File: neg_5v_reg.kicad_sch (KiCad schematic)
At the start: 33 parts, among them U2 SIC461ED-T1-GE3

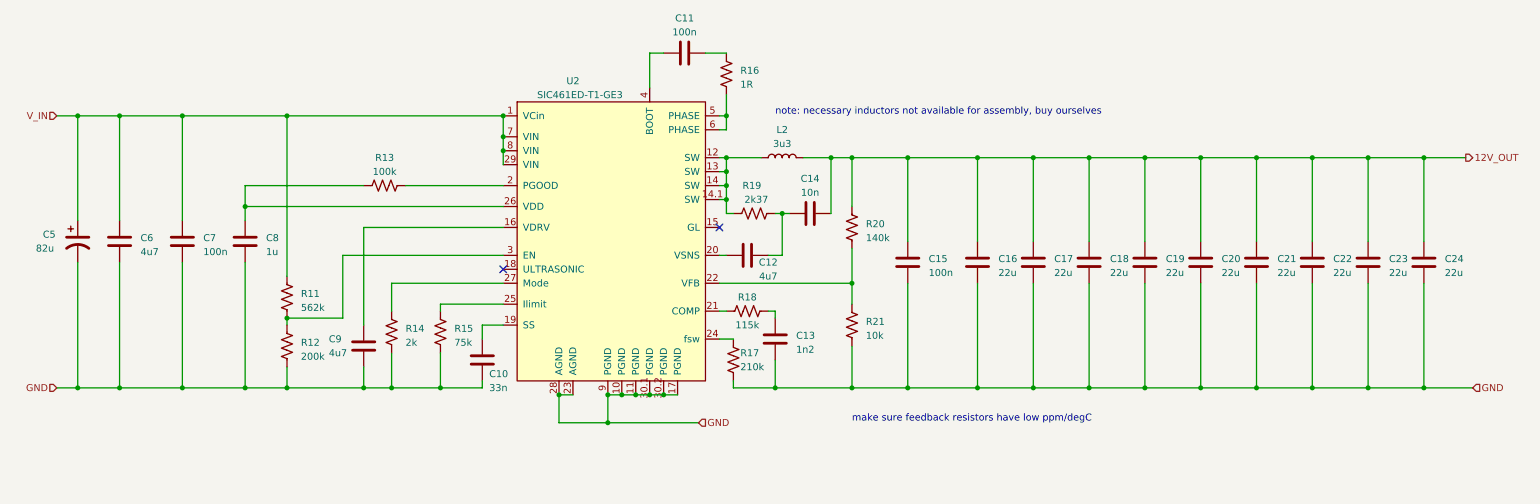
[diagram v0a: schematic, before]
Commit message: Added -5V voltage source using 5V regulator, also fixed 3V3 output pins on 3V3 regulator subsheets
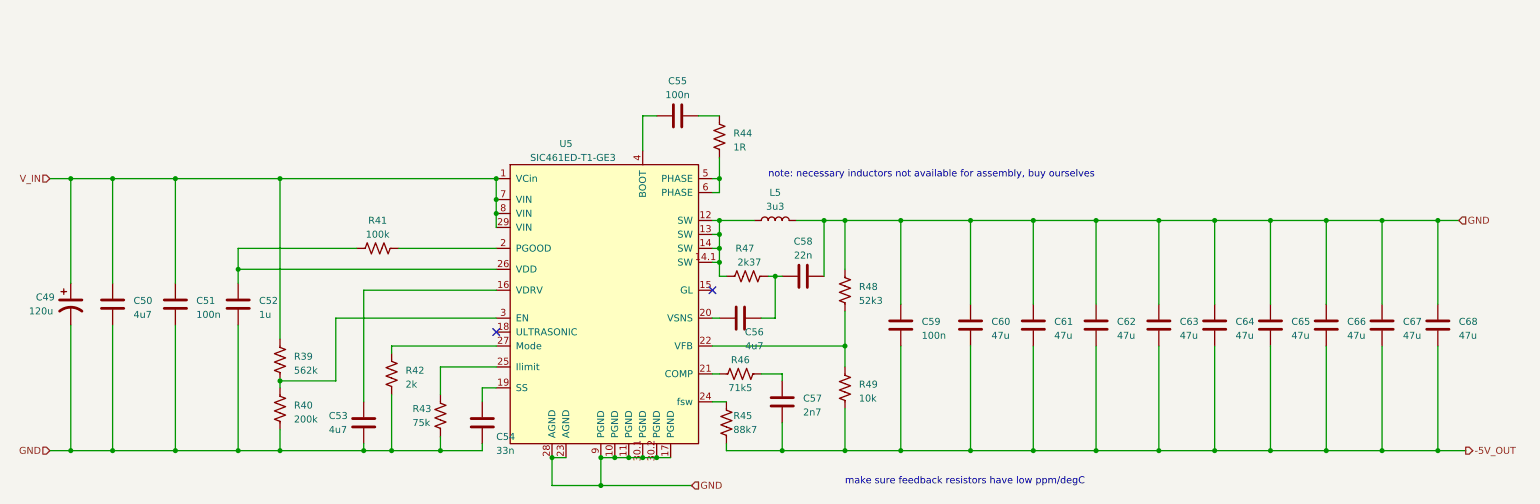
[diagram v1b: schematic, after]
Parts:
- removed C10: 33n, Capacitor_SMD:C_0603_1608Metric, symbol Device:C
- removed C11: 100n, Capacitor_SMD:C_0402_1005Metric, symbol Device:C
- removed C12, C9: 4u7, Capacitor_SMD:C_0805_2012Metric, symbol Device:C
- removed C13: 1n2, Capacitor_SMD:C_0603_1608Metric, symbol Device:C
- removed C14: 10n, Capacitor_SMD:C_0402_1005Metric, symbol Device:C
- removed C15, C7: 100n, Capacitor_SMD:C_0603_1608Metric, symbol Device:C
- removed C16, C17, C18, C19, C20, C21, C22, C23, C24: 22u, Capacitor_SMD:C_1210_3225Metric, symbol Device:C
- removed C5: 82u, Capacitor_THT:CP_Radial_D8.0mm_P3.50mm, symbol Device:C_Polarized_US
- removed C6: 4u7, Capacitor_SMD:C_0603_1608Metric, symbol Device:C
- removed C8: 1u, Capacitor_SMD:C_0603_1608Metric, symbol Device:C
- removed L2: 3u3, crush-power-footprints:IND_IHLP-6767GZ_VIS-M, symbol Device:L
- removed R11: 562k, Resistor_SMD:R_0603_1608Metric, symbol Device:R_US
- removed R12: 200k, Resistor_SMD:R_0603_1608Metric, symbol Device:R_US
- removed R13: 100k, Resistor_SMD:R_0603_1608Metric, symbol Device:R_US
- removed R14: 2k, Resistor_SMD:R_0603_1608Metric, symbol Device:R_US
- removed R15: 75k, Resistor_SMD:R_0603_1608Metric, symbol Device:R_US
- removed R16: 1R, Resistor_SMD:R_0402_1005Metric, symbol Device:R_US
- removed R17: 210k, Resistor_SMD:R_0603_1608Metric, symbol Device:R_US
- removed R18: 115k, Resistor_SMD:R_0402_1005Metric, symbol Device:R_US
- removed R19: 2k37, Resistor_SMD:R_0402_1005Metric, symbol Device:R_US
- removed R20: 140k, Resistor_SMD:R_0603_1608Metric, symbol Device:R_US
- removed R21: 10k, Resistor_SMD:R_0603_1608Metric, symbol Device:R_US
- removed U2: SIC461ED-T1-GE3, CONV_SIC461ED-T1-GE3, symbol crush-power-lib:SIC461ED-T1-GE3
- added C49: 120u, Capacitor_THT:CP_Radial_D8.0mm_P3.50mm, symbol Device:C_Polarized_US
- added C50: 4u7, Capacitor_SMD:C_0603_1608Metric, symbol Device:C
- added C51, C59: 100n, Capacitor_SMD:C_0603_1608Metric, symbol Device:C
- added C52: 1u, Capacitor_SMD:C_0603_1608Metric, symbol Device:C
- added C53, C56: 4u7, Capacitor_SMD:C_0805_2012Metric, symbol Device:C
- added C54: 33n, Capacitor_SMD:C_0603_1608Metric, symbol Device:C
- added C55: 100n, Capacitor_SMD:C_0402_1005Metric, symbol Device:C
- added C57: 2n7, Capacitor_SMD:C_0603_1608Metric, symbol Device:C
- added C58: 22n, Capacitor_SMD:C_0402_1005Metric, symbol Device:C
- added C60, C61, C62, C63, C64, C65, C66, C67, C68: 47u, Capacitor_SMD:C_1210_3225Metric, symbol Device:C
- added L5: 3u3, crush-power-footprints:IND_IHLP-6767GZ_VIS-M, symbol Device:L
- added R39: 562k, Resistor_SMD:R_0603_1608Metric, symbol Device:R_US
- added R40: 200k, Resistor_SMD:R_0603_1608Metric, symbol Device:R_US
- added R41: 100k, Resistor_SMD:R_0603_1608Metric, symbol Device:R_US
- added R42: 2k, Resistor_SMD:R_0603_1608Metric, symbol Device:R_US
- added R43: 75k, Resistor_SMD:R_0603_1608Metric, symbol Device:R_US
- added R44: 1R, Resistor_SMD:R_0402_1005Metric, symbol Device:R_US
- added R45: 88k7, Resistor_SMD:R_0603_1608Metric, symbol Device:R_US
- added R46: 71k5, Resistor_SMD:R_0402_1005Metric, symbol Device:R_US
- added R47: 2k37, Resistor_SMD:R_0402_1005Metric, symbol Device:R_US
- added R48: 52k3, Resistor_SMD:R_0603_1608Metric, symbol Device:R_US
- added R49: 10k, Resistor_SMD:R_0603_1608Metric, symbol Device:R_US
- added U5: SIC461ED-T1-GE3, CONV_SIC461ED-T1-GE3, symbol crush-power-lib:SIC461ED-T1-GE3
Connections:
- net GND: now also C49.2, C50.1, C51.1, C52.1, C53.1, C54.1, C58.2, C59.1, C60.1, C61.1, C62.1, C63.1, C64.1, C65.1, C66.1, C67.1, C68.1, L5.2, R40.1, R42.2, R43.2, R48.1, U5.10 (PGND), U5.11 (PGND), U5.17 (PGND), U5.23 (AGND), U5.28 (AGND), U5.30.1 (PGND), U5.30.2 (PGND), U5.9 (PGND)
- net V_IN: now also C49.1, C50.2, C51.2, R39.2, U5.1 (VCin), U5.29 (VIN), U5.7 (VIN), U5.8 (VIN)
- new net: R44.1, U5.5 (PHASE), U5.6 (PHASE)
- new net: C55.2, R44.2
- new net: C56.2, C58.1, R47.2
- new net: C54.2, U5.19 (SS)
- new net: C55.1, U5.4 (BOOT)
- new net: C56.1, U5.20 (VSNS)
- new net: R46.1, U5.21 (COMP)
- new net: C57.1, R46.2
- new net: C53.2, U5.16 (VDRV)
- new net: R45.1, U5.24 (fsw)
- new net: C52.2, R41.1, U5.26 (VDD)
- new net: L5.1, R47.1, U5.12 (SW), U5.13 (SW), U5.14 (SW), U5.14.1 (SW)
- new net: R48.2, R49.1, U5.22 (VFB)
- new net: R41.2, U5.2 (PGOOD)
- new net: R43.1, U5.25 (Ilimit)
- new net: R42.1, U5.27 (Mode)
- new net: R39.1, R40.2, U5.3 (EN)
- new net -5V_OUT: C57.2, C59.2, C60.2, C61.2, C62.2, C63.2, C64.2, C65.2, C66.2, C67.2, C68.2, R45.2, R49.2
